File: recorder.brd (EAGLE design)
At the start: 22.4 x 41 mm, 46 parts, among them M1 ELECTRET_MICROPHON-WM-61A, Q1 4.096MHz, T1 MMBT3904 NPN, U1 ISD15100

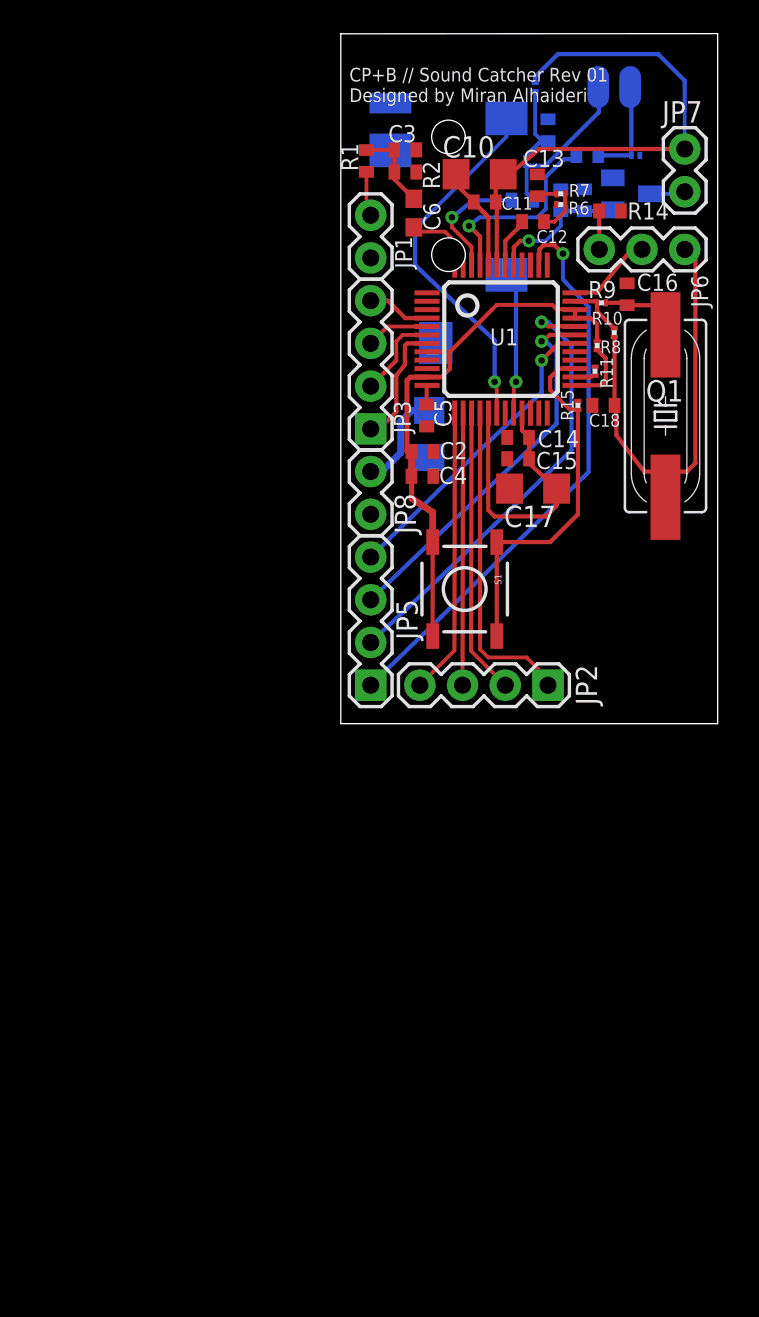
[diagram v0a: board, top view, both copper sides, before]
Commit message: upodated BOM. changed mic, headphone jack, and other passive components
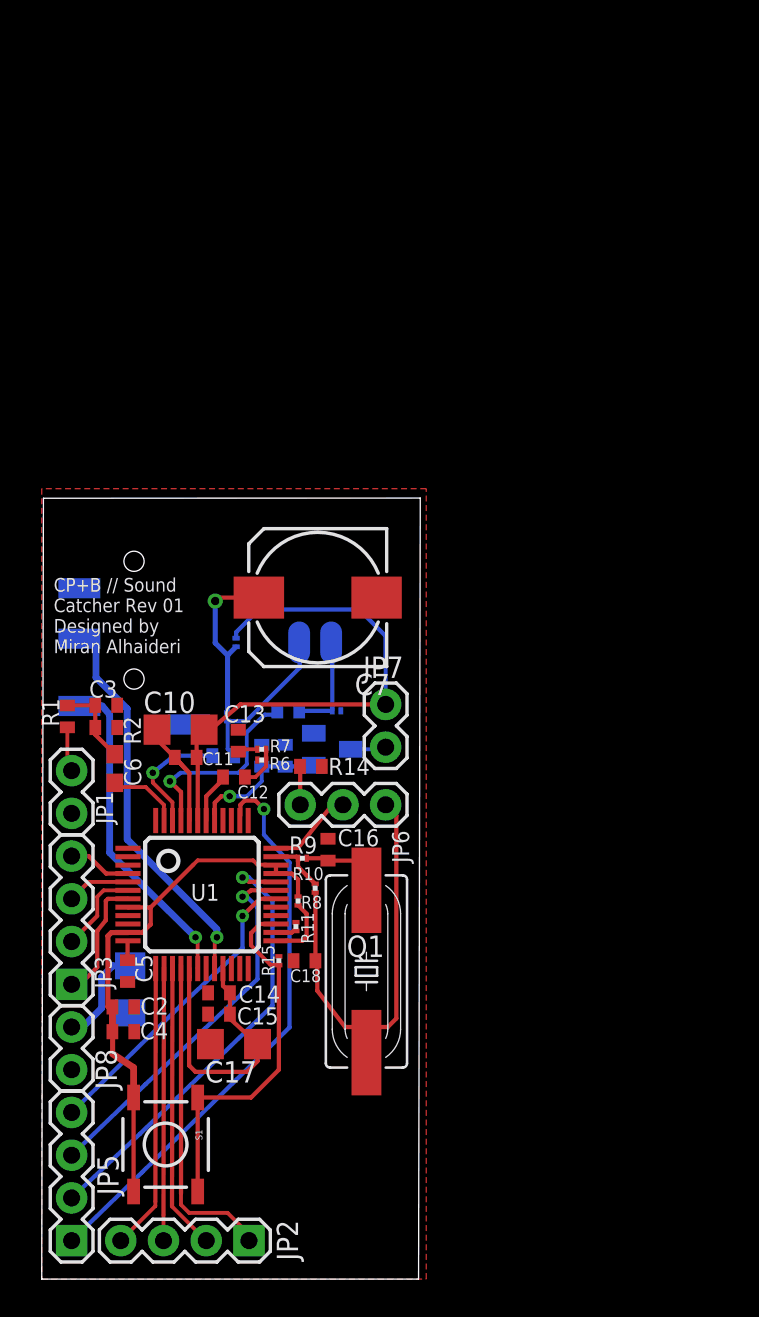
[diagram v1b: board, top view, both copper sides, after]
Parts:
- removed JP4: (no value), SparkFun-Connectors:AUDIO-JACK-3.5MM-SMD
- added U$1: AUDIO-JACK3, SparkFun-Connectors:AUDIO-JACK-TRRS-SMD
- C7: device rcl:C0402 -> rcl:175TMP-0808
- moved C16 37.5 mm to (22.1, 31.9)
- moved C10 37.5 mm to (13.3, 39.0)
- moved C12 37.5 mm to (16.5, 36.2)
- moved C15 37.5 mm to (15.6, 22.1)
- moved C17 37.5 mm to (16.5, 20.3)
- moved C3 37.5 mm to (8.92, 39.1)
- moved C9 37.5 mm to (19.7, 40.1)
- moved JP7 37.5 mm to (25.5, 40.5)
- moved JP8 37.5 mm to (6.86, 18.8)
- moved R11 37.5 mm to (20.2, 27.3)
- moved R2 37.5 mm to (8.92, 40.5)
- moved R4 37.5 mm to (16.1, 39.8)
- moved R5 37.5 mm to (22.6, 40.1)
- moved R7 37.5 mm to (18.2, 37.8)
- moved S1 37.5 mm to (12.4, 14.4)
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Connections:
- net GND: now also C7.-, U$1.EARTH; no longer C7.2
- net N$28: now also C7.+; no longer C7.1
- net SPK+: now also U$1.TIP; no longer JP4.SLEEVE
- net SPK-: now also U$1.RING1; no longer JP4.TIP
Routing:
- net SPK-: track 8.51 -> 22.7 mm
- net N$28: track 4.55 -> 10.3 mm, vias 0 -> 1
- net SPK+: track 21.8 -> 19.3 mm
- added copper zone on layer 1, net N$16
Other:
- board size 22.4 x 41 mm -> 22.5 x 46.4 mm

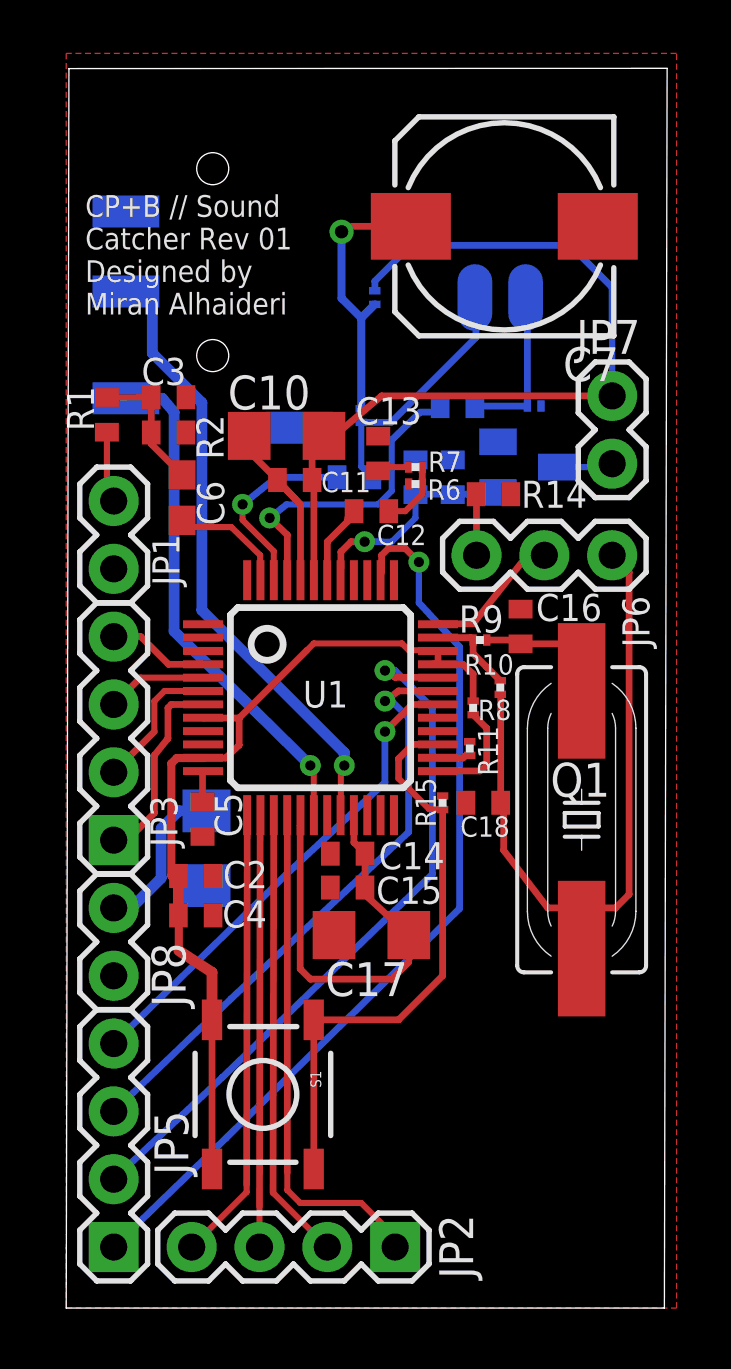
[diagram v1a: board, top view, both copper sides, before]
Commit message: moved gnd plane to bottom layer, added vias to gnd, and adjust components around to pass DRC
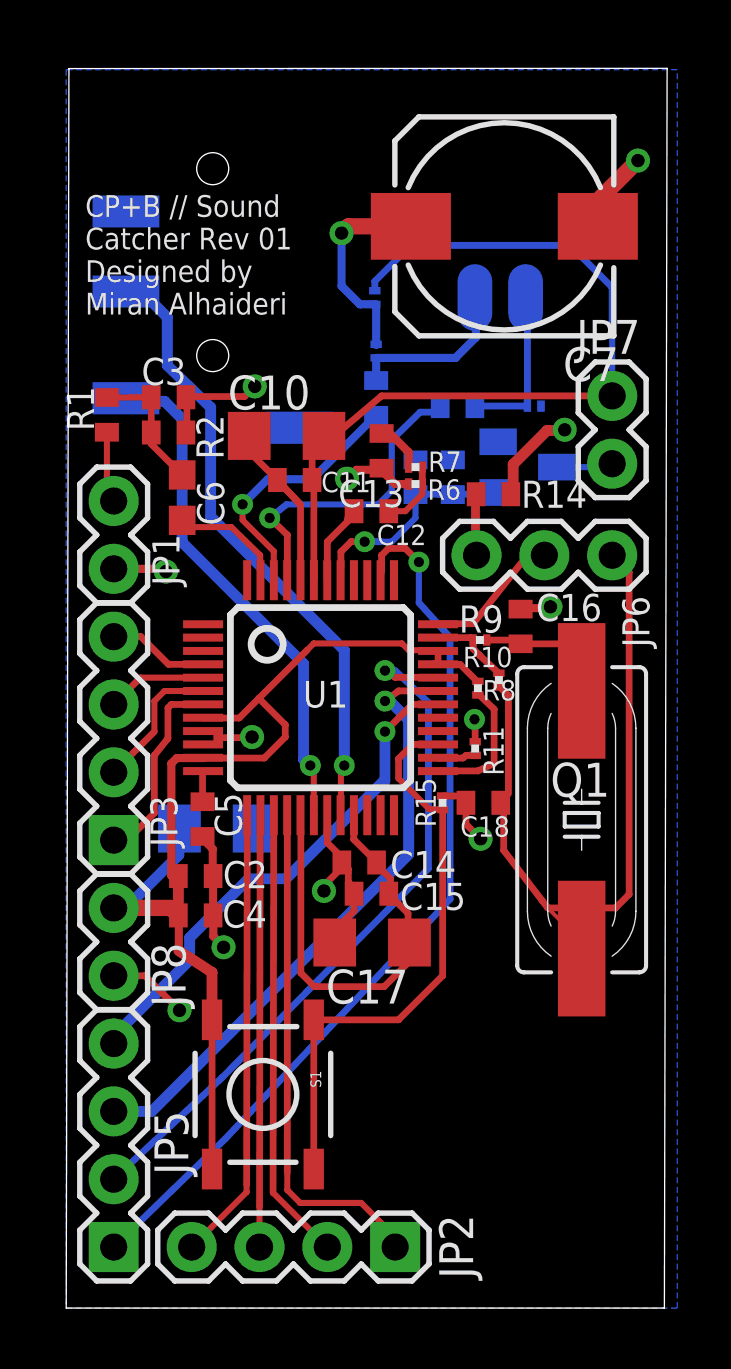
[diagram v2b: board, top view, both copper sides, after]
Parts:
- moved C8 3.08 mm to (16.7, 40.4), turned to 90 degrees
- moved R4 2.48 mm to (16.7, 42.2)
- moved C15 0.92 mm to (16.5, 21.9)
- moved C1 0.83 mm to (10.7, 24.3), turned to 180 degrees
- moved R8 0.76 mm to (20.5, 29.6)
- moved C14 0.54 mm to (16.1, 23.0)
- moved R10 0.28 mm to (21.3, 29.9)
- moved C17 0.28 mm to (16.5, 20.0)
- moved R11 0.20 mm to (20.4, 27.3)
- moved C13 0.16 mm to (16.9, 38.5), turned to 270 degrees
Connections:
- net GPIO2 renamed N$21
- net VCCD renamed N$27
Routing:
- net GND: track 0.00 -> 33.4 mm, vias 0 -> 12
- net N$7: track 2.16 -> 5.09 mm
- net VCCD_PWM: track 16.3 -> 13.8 mm
- net MIC+: track 7.22 -> 9.71 mm
- net N$1: track 26.5 -> 29.0 mm
- net N$28: track 10.3 -> 7.98 mm
- net N$22: track 8.35 -> 6.44 mm
- net N$27: track 39.1 -> 40.6 mm
- net AUDOUT: track 7.96 -> 9.23 mm
- net SPK+: track 19.3 -> 18.3 mm
- net N$4: track 3.46 -> 4.41 mm
- net GPIO3: track 17.8 -> 18.5 mm
- net N$21: track 22.2 -> 22.8 mm
- added copper zone on layer 16, net GND
- removed copper zone on layer 1, net N$16
